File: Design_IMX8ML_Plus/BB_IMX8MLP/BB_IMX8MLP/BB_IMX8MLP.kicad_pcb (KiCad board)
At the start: 2 copper layers, 6 parts, among them J1 DF40C-100DP-0.4V_51_, J2 DF40C-100DP-0.4V_51_, J3 DF40C-100DP-0.4V_51_, J4 DF40C-100DP-0.4V_51_, J5 RJ45_Amphenol_RJMG1BD3B8K1ANR, J6 RJ45_Amphenol_RJMG1BD3B8K1ANR

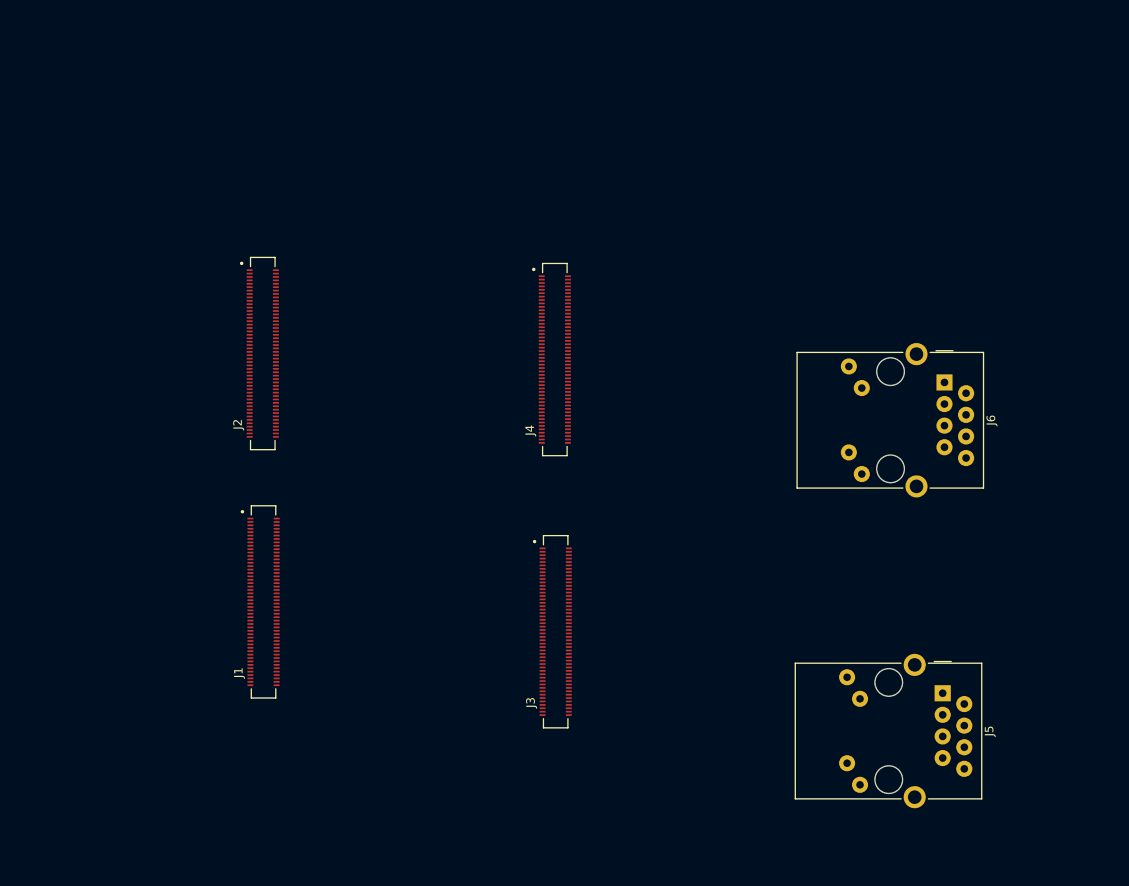
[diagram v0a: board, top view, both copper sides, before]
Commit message: Add SPB228 WIFI/BLE module
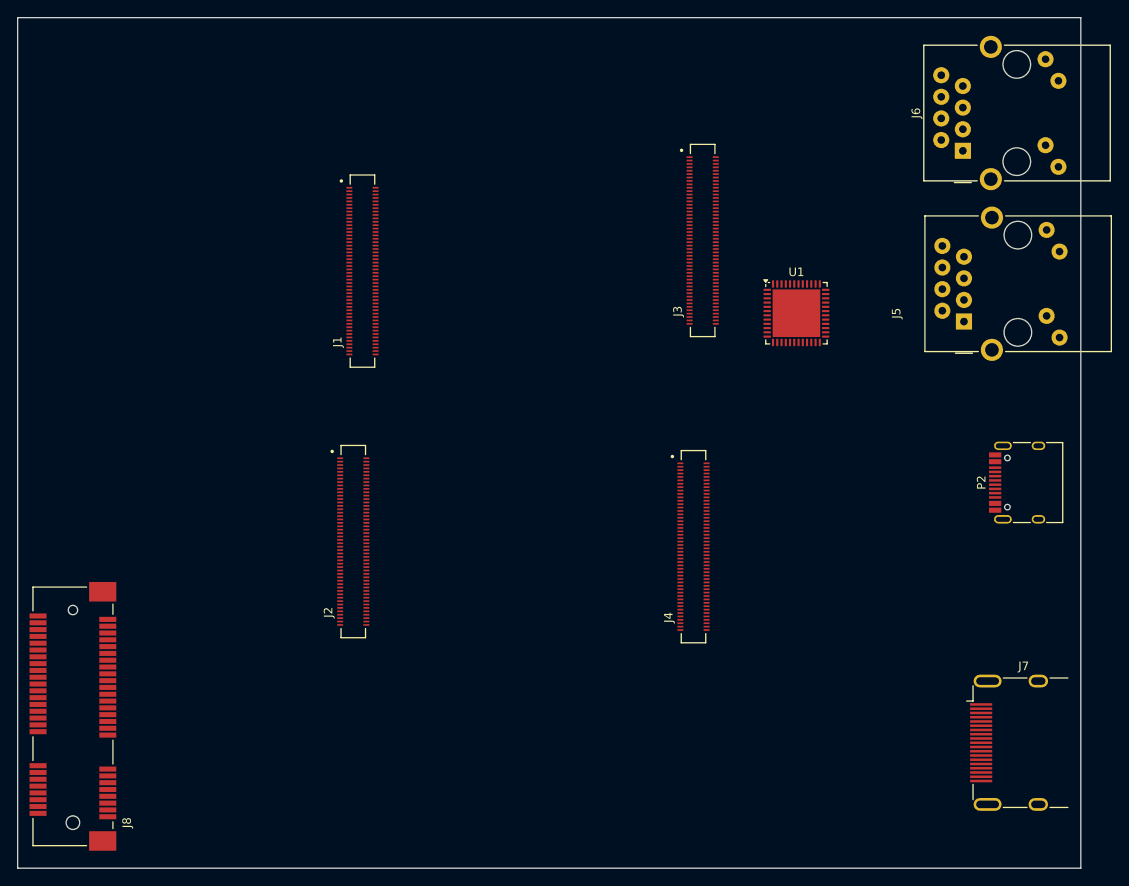
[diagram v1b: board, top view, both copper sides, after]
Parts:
- added J7: HDMI_A, Connector_Video:HDMI_A_Molex_208658-1001_Horizontal, F.Cu at (186.6, 135.2)
- added J8: Bus_PCI_Express_Mini, Connector_PCBEdge:BUS_PCI_Express_Mini, F.Cu at (76.5, 132.2)
- added P2: USB_C_Plug, Connector_USB:USB_C_Receptacle_HRO_TYPE-C-31-M-12, F.Cu at (189.0, 104.7)
- added U1: KSZ9131RNXI, Package_DFN_QFN:QFN-48-1EP_7x7mm_P0.5mm_EP5.6x5.6mm, F.Cu at (161.6, 84.8)
- moved J3 49.1 mm to (150.5, 76.2)
- moved J5 43.8 mm to (181.3, 85.7), turned to 90 degrees
- moved J1 40.6 mm to (110.5, 79.8)
- moved J4 27.4 mm to (149.5, 112.2)
- moved J6 27.3 mm to (181.1, 65.7), turned to 90 degrees
- moved J2 24.5 mm to (109.5, 111.6)
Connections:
- J1 pad 29: unconnected-(J1-Pad29) -> SAI1_RXD5
- J1 pad 31: unconnected-(J1-Pad31) -> SAI1_RXD6
- J1 pad 32: unconnected-(J1-Pad32) -> SAI5_RXD0
- J1 pad 33: unconnected-(J1-Pad33) -> SAI1_RXD7
- J1 pad 34: unconnected-(J1-Pad34) -> SAI5_RXD1
- J1 pad 35: unconnected-(J1-Pad35) -> SAI1_TXD0
- J1 pad 36: unconnected-(J1-Pad36) -> SAI5_RXD2
- J1 pad 37: unconnected-(J1-Pad37) -> SAI1_TXD1
- J1 pad 38: unconnected-(J1-Pad38) -> SAI5_RXD3
- J1 pad 39: unconnected-(J1-Pad39) -> SAI1_TXD2
- J1 pad 40: unconnected-(J1-Pad40) -> SAI5_MCLK
- J1 pad 41: unconnected-(J1-Pad41) -> SAI1_TXD3
- J1 pad 42: unconnected-(J1-Pad42) -> SAI5_RXC
- J1 pad 43: unconnected-(J1-Pad43) -> SAI1_TXD4
- J1 pad 44: unconnected-(J1-Pad44) -> SAI5_RXFS
- J1 pad 45: unconnected-(J1-Pad45) -> SAI1_TXD5
- J1 pad 47: unconnected-(J1-Pad47) -> SAI1_TXD6
- J1 pad 49: unconnected-(J1-Pad49) -> SAI1_RXD7
- J1 pad 60: unconnected-(J1-Pad60) -> LED1
- J1 pad 62: unconnected-(J1-Pad62) -> LED2
- J1 pad 66: unconnected-(J1-Pad66) -> TXRXA_N
- J1 pad 68: unconnected-(J1-Pad68) -> TXRXA_P
- J1 pad 72: unconnected-(J1-Pad72) -> TXRXB_N
- J1 pad 74: unconnected-(J1-Pad74) -> TXRXB_P
- J1 pad 78: unconnected-(J1-Pad78) -> TXRXC_P
- J1 pad 80: unconnected-(J1-Pad80) -> TXRXC_N
- J1 pad 84: unconnected-(J1-Pad84) -> TXRXD_N
- J1 pad 86: unconnected-(J1-Pad86) -> TXRXD_P
- J2 pad 10: unconnected-(J2-Pad10) -> SAI2_MCLK
- J2 pad 11: unconnected-(J2-Pad11) -> SAI1_MCLK
- J2 pad 12: unconnected-(J2-Pad12) -> SAI2_RXC
- J2 pad 13: unconnected-(J2-Pad13) -> SAI1_RXC
- J2 pad 14: unconnected-(J2-Pad14) -> SAI2_RXFS
- J2 pad 15: unconnected-(J2-Pad15) -> SAI1_RXFS
- J2 pad 16: unconnected-(J2-Pad16) -> SAI2_TXC
- J2 pad 17: unconnected-(J2-Pad17) -> SAI1_TXC
- J2 pad 18: unconnected-(J2-Pad18) -> SAI2_TXFS
- J2 pad 19: unconnected-(J2-Pad19) -> SAi1_TXFS
- J2 pad 21: unconnected-(J2-Pad21) -> I2C1_SCL
- J2 pad 22: unconnected-(J2-Pad22) -> SAI2_RXD0
- J2 pad 23: unconnected-(J2-Pad23) -> I2C1_SDA
- J2 pad 24: unconnected-(J2-Pad24) -> SAI2_TXD0
- J2 pad 27: unconnected-(J2-Pad27) -> I2C3_SDA
- J2 pad 28: unconnected-(J2-Pad28) -> SAI3_MCLK
- J2 pad 29: unconnected-(J2-Pad29) -> I2C3_SCL
- J2 pad 30: unconnected-(J2-Pad30) -> SAI3_RXC
- J2 pad 32: unconnected-(J2-Pad32) -> SAI3_RXD
- J2 pad 33: unconnected-(J2-Pad33) -> I2C2_SCL
- J2 pad 34: unconnected-(J2-Pad34) -> SAI3_RXFS
- J2 pad 35: unconnected-(J2-Pad35) -> I2C2_SDA
- J2 pad 36: unconnected-(J2-Pad36) -> SAI3_TXC
- J2 pad 38: unconnected-(J2-Pad38) -> SAI3_TXD
- J2 pad 39: unconnected-(J2-Pad39) -> I2C4_SDA
- J2 pad 40: unconnected-(J2-Pad40) -> SAI3_TXFS
- J2 pad 41: unconnected-(J2-Pad41) -> I2C4_SCL
- J2 pad 45: unconnected-(J2-Pad45) -> UART1_RXD
- J2 pad 47: unconnected-(J2-Pad47) -> UART1_TXD
- J2 pad 48: unconnected-(J2-Pad48) -> SAI1_RXD0
- J2 pad 49: unconnected-(J2-Pad49) -> UART2_RXD
- J2 pad 50: unconnected-(J2-Pad50) -> SAI1_RXD1
- J2 pad 51: unconnected-(J2-Pad51) -> UART2_TXD
- J2 pad 52: unconnected-(J2-Pad52) -> SAI1_RXD2
- J2 pad 53: unconnected-(J2-Pad53) -> UART3_RXD
- J2 pad 54: unconnected-(J2-Pad54) -> SAI1_RXD3
- J2 pad 55: unconnected-(J2-Pad55) -> UART3_TXD
- J2 pad 56: unconnected-(J2-Pad56) -> SAI1_RXD4
- J2 pad 57: unconnected-(J2-Pad57) -> UART4_RXD
- J2 pad 59: unconnected-(J2-Pad59) -> UART4_TXD
- J2 pad 65: unconnected-(J2-Pad65) -> CSI1_CLK_P
- J2 pad 67: unconnected-(J2-Pad67) -> CSI1_CLK_N
- J2 pad 71: unconnected-(J2-Pad71) -> CSI2_CLK_P
- J2 pad 73: unconnected-(J2-Pad73) -> CSI2_CLK_N
- J2 pad 77: unconnected-(J2-Pad77) -> DSI1_CLK_P
- J2 pad 79: unconnected-(J2-Pad79) -> DSI1_CLK_N
- J2 pad 80: unconnected-(J2-Pad80) -> ECSPI1_MISO
- J2 pad 82: unconnected-(J2-Pad82) -> ECSPI1_MOSI
- J2 pad 84: unconnected-(J2-Pad84) -> ECSPI1_SCLK
- J2 pad 85: unconnected-(J2-Pad85) -> EARC_AUX
- J2 pad 86: unconnected-(J2-Pad86) -> ECSPI1_SSO
- J2 pad 87: unconnected-(J2-Pad87) -> EARC_N_HPD
- J2 pad 88: unconnected-(J2-Pad88) -> ECSPI2_MISO
- J2 pad 89: unconnected-(J2-Pad89) -> EARC_P_UTIL
- J2 pad 90: unconnected-(J2-Pad90) -> ECSPI2_MOSI
- J2 pad 92: unconnected-(J2-Pad92) -> ECSPI2_SCLK
- J2 pad 94: unconnected-(J2-Pad94) -> ECSPI2_SSO
- J3 pad 100: unconnected-(J3-Pad100) -> VDD_SYS
- J3 pad 11: unconnected-(J3-Pad11) -> PCIE_TXN_P
- J3 pad 13: unconnected-(J3-Pad13) -> PCIE_TXN_N
- J3 pad 15: unconnected-(J3-Pad15) -> PCIE_RXN_P
- J3 pad 17: unconnected-(J3-Pad17) -> PCIE_RXN_N
- J3 pad 21: unconnected-(J3-Pad21) -> PCIE_REF_PAD_CLK_P
- J3 pad 23: unconnected-(J3-Pad23) -> PCIE_REF_PAD_CLK_N
- J3 pad 33: unconnected-(J3-Pad33) -> GPIO1_IO00
- J3 pad 35: unconnected-(J3-Pad35) -> GPIO1_IO01
- J3 pad 37: unconnected-(J3-Pad37) -> GPIO1_IO02
- J3 pad 43: unconnected-(J3-Pad43) -> GPIO1_IO05
- J3 pad 45: unconnected-(J3-Pad45) -> GPIO1_IO06
- J3 pad 47: unconnected-(J3-Pad47) -> GPIO1_IO07
- J3 pad 49: unconnected-(J3-Pad49) -> GPIO1_IO08
- J3 pad 51: unconnected-(J3-Pad51) -> GPIO1_IO09
- J3 pad 53: unconnected-(J3-Pad53) -> GPIO1_IO10
- J3 pad 55: unconnected-(J3-Pad55) -> GPIO1_IO11
- J3 pad 57: unconnected-(J3-Pad57) -> GPIO1_IO12
- J3 pad 59: unconnected-(J3-Pad59) -> GPIO1_IO13
- J3 pad 61: unconnected-(J3-Pad61) -> GPIO1_IO14
- J3 pad 63: unconnected-(J3-Pad63) -> GPIO1_IO15
- J3 pad 75: unconnected-(J3-Pad75) -> GND
- J3 pad 76: unconnected-(J3-Pad76) -> GND
- J3 pad 77: unconnected-(J3-Pad77) -> GND
- J3 pad 78: unconnected-(J3-Pad78) -> GND
- J3 pad 79: unconnected-(J3-Pad79) -> GND
- J3 pad 80: unconnected-(J3-Pad80) -> GND
- J3 pad 81: unconnected-(J3-Pad81) -> GND
- J3 pad 82: unconnected-(J3-Pad82) -> GND
- J3 pad 83: unconnected-(J3-Pad83) -> GND
- J3 pad 84: unconnected-(J3-Pad84) -> GND
- J3 pad 85: unconnected-(J3-Pad85) -> GND
- J3 pad 86: unconnected-(J3-Pad86) -> GND
- J3 pad 87: unconnected-(J3-Pad87) -> GND
- J3 pad 88: unconnected-(J3-Pad88) -> GND
- J3 pad 89: unconnected-(J3-Pad89) -> VDD_SYS
- J3 pad 90: unconnected-(J3-Pad90) -> VDD_SYS
- J3 pad 91: unconnected-(J3-Pad91) -> VDD_SYS
- J3 pad 92: unconnected-(J3-Pad92) -> VDD_SYS
- J3 pad 93: unconnected-(J3-Pad93) -> VDD_SYS
- J3 pad 94: unconnected-(J3-Pad94) -> VDD_SYS
- J3 pad 95: unconnected-(J3-Pad95) -> VDD_SYS
- J3 pad 96: unconnected-(J3-Pad96) -> VDD_SYS
- J3 pad 97: unconnected-(J3-Pad97) -> VDD_SYS
- J3 pad 98: unconnected-(J3-Pad98) -> VDD_SYS
- J3 pad 99: unconnected-(J3-Pad99) -> VDD_SYS
- J4 pad 10: unconnected-(J4-Pad10) -> JTAG_TMS
- J4 pad 11: unconnected-(J4-Pad11) -> HDM_TX2_N
- J4 pad 12: unconnected-(J4-Pad12) -> JTAG_TDO
- J4 pad 13: unconnected-(J4-Pad13) -> HDM_TX1_P
- J4 pad 14: unconnected-(J4-Pad14) -> JTAG_TDI
- J4 pad 15: unconnected-(J4-Pad15) -> HDM_TX1_N
- J4 pad 16: unconnected-(J4-Pad16) -> JTAG_TCK
- J4 pad 17: unconnected-(J4-Pad17) -> HDM_TX0_P
- J4 pad 18: unconnected-(J4-Pad18) -> JTAG_MOD
- J4 pad 19: unconnected-(J4-Pad19) -> HDM_TX0_N
- J4 pad 22: unconnected-(J4-Pad22) -> CLKOUT2
- J4 pad 23: unconnected-(J4-Pad23) -> HDM_HPD
- J4 pad 24: unconnected-(J4-Pad24) -> CLKOUT1
- J4 pad 25: unconnected-(J4-Pad25) -> HDM_DDC_SDA
- J4 pad 26: unconnected-(J4-Pad26) -> CLKIN2
- J4 pad 27: unconnected-(J4-Pad27) -> HDM_DDC_SCL
- J4 pad 28: unconnected-(J4-Pad28) -> CLKIN1
- J4 pad 29: unconnected-(J4-Pad29) -> HDM_CEC
- J4 pad 32: unconnected-(J4-Pad32) -> BOOT_MODE3
- J4 pad 34: unconnected-(J4-Pad34) -> BOOT_MODE2
- J4 pad 36: unconnected-(J4-Pad36) -> BOOT_MODE1
- J4 pad 37: unconnected-(J4-Pad37) -> LVDS1_CLK_N
- J4 pad 38: unconnected-(J4-Pad38) -> BOOT_MODE0
- J4 pad 39: unconnected-(J4-Pad39) -> LVDS1_CLK_P
- J4 pad 41: unconnected-(J4-Pad41) -> LVDS1_D3_P
- J4 pad 43: unconnected-(J4-Pad43) -> LVDS1_D3_N
- J4 pad 44: unconnected-(J4-Pad44) -> SDC1_STROBE
- J4 pad 45: unconnected-(J4-Pad45) -> LVDS1_D2_P
- J4 pad 46: unconnected-(J4-Pad46) -> SDC1_RESET_B
- J4 pad 47: unconnected-(J4-Pad47) -> LVDS1_D2_N
- J4 pad 48: unconnected-(J4-Pad48) -> SDC1_DATA7
- J4 pad 49: unconnected-(J4-Pad49) -> LVDS1_D1_P
- J4 pad 5: unconnected-(J4-Pad5) -> HDM_TXC_P
- J4 pad 50: unconnected-(J4-Pad50) -> SDC1_DATA6
- J4 pad 51: unconnected-(J4-Pad51) -> LVDS1_D1_N
- J4 pad 52: unconnected-(J4-Pad52) -> SDC1_DATA5
- J4 pad 53: unconnected-(J4-Pad53) -> LVDS1_D0_P
- J4 pad 54: unconnected-(J4-Pad54) -> SDC1_DATA4
- J4 pad 55: unconnected-(J4-Pad55) -> LVDS1_D0_N
- J4 pad 56: unconnected-(J4-Pad56) -> SDC1_DATA3
- J4 pad 58: unconnected-(J4-Pad58) -> SDC1_DATA2
- J4 pad 59: unconnected-(J4-Pad59) -> LVDS0_CLK_P
- J4 pad 60: unconnected-(J4-Pad60) -> SDC1_DATA1
- J4 pad 61: unconnected-(J4-Pad61) -> LVDS0_CLK_N
- J4 pad 62: unconnected-(J4-Pad62) -> SDC1_DATA0
- J4 pad 63: unconnected-(J4-Pad63) -> LVDS0_D3_P
- J4 pad 64: unconnected-(J4-Pad64) -> SDC1_CMD
- J4 pad 65: unconnected-(J4-Pad65) -> LVDS0_D3_N
- J4 pad 66: unconnected-(J4-Pad66) -> SDC1_CLK
- J4 pad 67: unconnected-(J4-Pad67) -> LVDS0_D2_P
- J4 pad 69: unconnected-(J4-Pad69) -> LVDS0_D2_N
- J4 pad 7: unconnected-(J4-Pad7) -> HDM_TXC_N
- J4 pad 70: unconnected-(J4-Pad70) -> SDC2_WP
- J4 pad 71: unconnected-(J4-Pad71) -> LVDS0_D1_P
- J4 pad 72: unconnected-(J4-Pad72) -> SDC2_RESET_B
- J4 pad 73: unconnected-(J4-Pad73) -> LVDS0_D1_N
- J4 pad 74: unconnected-(J4-Pad74) -> SDC2_DATA3
- J4 pad 75: unconnected-(J4-Pad75) -> LVDS0_D0_P
- J4 pad 76: unconnected-(J4-Pad76) -> SDC2_DATA2
- J4 pad 77: unconnected-(J4-Pad77) -> LVDS0_D0_N
- J4 pad 78: unconnected-(J4-Pad78) -> SDC2_DATA1
- J4 pad 80: unconnected-(J4-Pad80) -> SDC2_DATA0
- J4 pad 82: unconnected-(J4-Pad82) -> SDC2_CMD
- J4 pad 84: unconnected-(J4-Pad84) -> SDC2_CLK
- J4 pad 86: unconnected-(J4-Pad86) -> SDC2_CD_B
- J4 pad 9: unconnected-(J4-Pad9) -> HDM_TX2_P
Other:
- board outline added: 125 x 100 mm

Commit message: Improve power source module in the base board
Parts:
- added C1: 16Pf, Capacitor_SMD:C_0402_1005Metric, F.Cu at (168.2, 120.0)
- added C10: 100nF, Capacitor_SMD:C_0402_1005Metric, B.Cu at (66.4, 171.0)
- added C11: 10uF, Capacitor_SMD:C_0402_1005Metric, F.Cu at (63.0, 177.0)
- added C12: 100nF, Capacitor_SMD:C_0402_1005Metric, F.Cu at (64.0, 178.7)
- added C13: 1uF, Capacitor_SMD:C_0402_1005Metric, F.Cu at (70.1, 176.5)
- added C14: 10uF, Capacitor_SMD:C_0402_1005Metric, F.Cu at (67.5, 161.1)
- added C15: 10uF, Capacitor_SMD:C_0402_1005Metric, F.Cu at (67.4, 162.4)
- added C16: 10uF, Capacitor_SMD:C_0402_1005Metric, F.Cu at (67.4, 163.7)
- added C17: 47uF, Capacitor_SMD:C_0402_1005Metric, F.Cu at (41.2, 183.8)
- added C18: 47uF, Capacitor_SMD:C_0402_1005Metric, F.Cu at (41.1, 182.6)
- added C19: 47uF, Capacitor_SMD:C_0402_1005Metric, F.Cu at (41.1, 181.4)
- added C2: 16Pf, Capacitor_SMD:C_0402_1005Metric, F.Cu at (165.4, 120.3)
- added C20: 10uF, Capacitor_SMD:C_0402_1005Metric, F.Cu at (82.5, 174.8)
- added C21: 47uF, Capacitor_SMD:C_0402_1005Metric, F.Cu at (118.8, 174.4)
- added C22: 47uF, Capacitor_SMD:C_0402_1005Metric, F.Cu at (118.8, 176.4)
- added C23: 47uF, Capacitor_SMD:C_0402_1005Metric, F.Cu at (118.8, 178.3)
- added C24: 47uF, Capacitor_SMD:C_0402_1005Metric, F.Cu at (118.8, 180.3)
- added C25: 4.7uF, Capacitor_SMD:C_0402_1005Metric, F.Cu at (118.8, 182.3)
- added C26: 100nF, Capacitor_SMD:C_0402_1005Metric, F.Cu at (118.8, 184.2)
- added C27: 100nF, Capacitor_SMD:C_0402_1005Metric, F.Cu at (118.8, 186.2)
- added C28: 100nF, Capacitor_SMD:C_0402_1005Metric, B.Cu at (84.3, 135.4)
- added C3: 47uF, Capacitor_SMD:C_0402_1005Metric, F.Cu at (41.1, 185.0)
- added C4: 100nF, Capacitor_SMD:C_0402_1005Metric, F.Cu at (82.2, 167.8)
- added C5: 10uF, Capacitor_SMD:C_0402_1005Metric, B.Cu at (77.1, 164.8)
- added C6: 10uF, Capacitor_SMD:C_0402_1005Metric, F.Cu at (75.2, 177.5)
- added C7: 100nF, Capacitor_SMD:C_0402_1005Metric, F.Cu at (56.0, 186.0)
- added C8: 100nF, Capacitor_SMD:C_0402_1005Metric, B.Cu at (58.9, 185.9)
- added C9: 4.7uF, Capacitor_SMD:C_0402_1005Metric, F.Cu at (58.1, 186.7)
- added D1: SS3200, Diode_SMD:D_SMA, F.Cu at (80.6, 177.9)
- added D2: GREEN, LED_SMD:LED_0402_1005Metric, F.Cu at (85.5, 127.3)
- added D3: GREEN, LED_SMD:LED_0402_1005Metric, F.Cu at (85.5, 125.3)
- added D4: GREEN, LED_SMD:LED_0402_1005Metric, F.Cu at (85.5, 123.3)
- added F1: 10A 36R@100MHz, Fuse:Fuse_0603_1608Metric, F.Cu at (79.5, 175.0)
- added J10: Barrel_Jack, Connector_BarrelJack:BarrelJack_CUI_PJ-063AH_Horizontal, F.Cu at (78.3, 181.7)
- added J11: SIM_Card, Connector_Card:nanoSIM_Hinged_CUI_NSIM-2-C, B.Cu at (93.0, 139.5)
- added J9: GSB311231HR, _W_SBC:AMPHENOL_GSB311231HR, F.Cu at (183.8, 115.1)
- added L1: 2.2uH_12A, Inductor_SMD:L_7.3x7.3_H3.5, F.Cu at (47.5, 182.9)
- added L2: 2.2uH_12A, Inductor_SMD:L_7.3x7.3_H3.5, F.Cu at (124.9, 177.8)
- added Q1: PMDT290UCE, Package_TO_SOT_SMD:SOT-666, F.Cu at (66.7, 182.5)
- added Q2: NTMFS5C670NLT1G, _W_SBC:NTMFS5C670NLT1G_ONS, F.Cu at (72.8, 162.9)
- added Q3: NTMFS5C670NLT1G, _W_SBC:NTMFS5C670NLT1G_ONS, F.Cu at (82.0, 162.6)
- added Q4: PMDT290UCE, Package_TO_SOT_SMD:SOT-666, F.Cu at (128.1, 184.1)
- added R1: 47K, Resistor_SMD:R_0402_1005Metric, B.Cu at (58.8, 181.8)
- added R10: 100K, Resistor_SMD:R_0402_1005Metric, F.Cu at (84.4, 171.2)
- added R11: 787K, Resistor_SMD:R_0402_1005Metric, F.Cu at (84.4, 170.0)
- added R12: 80.6K, Resistor_SMD:R_0402_1005Metric, F.Cu at (84.4, 168.6)
- added R13: 18.2K, Resistor_SMD:R_0402_1005Metric, F.Cu at (84.4, 167.5)
- added R14: 80.6K, Resistor_SMD:R_0402_1005Metric, B.Cu at (79.0, 164.8)
- added R15: 0.01, Resistor_SMD:R_0402_1005Metric, F.Cu at (67.4, 164.8)
- added R16: 100K, Resistor_SMD:R_0402_1005Metric, F.Cu at (115.9, 174.4)
- added R17: 100K, Resistor_SMD:R_0402_1005Metric, F.Cu at (115.9, 176.4)
- added R18: 100K, Resistor_SMD:R_0402_1005Metric, F.Cu at (115.9, 178.4)
- added R19: 47K, Resistor_SMD:R_0402_1005Metric, F.Cu at (115.9, 180.4)
- added R2: 8.87K, Resistor_SMD:R_0402_1005Metric, B.Cu at (58.8, 180.6)
- added R20: 8.87K, Resistor_SMD:R_0402_1005Metric, F.Cu at (115.9, 182.4)
- added R21: 100K, Resistor_SMD:R_0402_1005Metric, F.Cu at (115.9, 184.3)
- added R22: 510K, Resistor_SMD:R_0402_1005Metric, F.Cu at (115.9, 186.3)
- added R23: 100K, Resistor_SMD:R_0402_1005Metric, F.Cu at (115.9, 188.3)
- added R24: 100K, Resistor_SMD:R_0402_1005Metric, F.Cu at (88.7, 127.3)
- added R25: 100K, Resistor_SMD:R_0402_1005Metric, F.Cu at (88.7, 125.3)
- added R26: 100K, Resistor_SMD:R_0402_1005Metric, F.Cu at (88.7, 123.3)
- added R3: 100K, Resistor_SMD:R_0402_1005Metric, F.Cu at (58.1, 185.6)
- added R4: 100K, Resistor_SMD:R_0402_1005Metric, F.Cu at (61.8, 182.3)
- added R5: 100K, Resistor_SMD:R_0402_1005Metric, F.Cu at (63.2, 184.3)
- added R6: 510K, Resistor_SMD:R_0402_1005Metric, F.Cu at (59.0, 178.8)
- added R7: 100K, Resistor_SMD:R_0402_1005Metric, F.Cu at (66.2, 178.7)
- added R8: 100K, Resistor_SMD:R_0402_1005Metric, F.Cu at (70.6, 183.3)
- added R9: 100K, Resistor_SMD:R_0402_1005Metric, F.Cu at (70.6, 182.0)
- added SW1: Power ON/OFF, Button_Switch_SMD:SW_SPST_TL3342, F.Cu at (95.9, 174.3)
- added SW2: RESET, Button_Switch_SMD:SW_SPST_TL3342, F.Cu at (95.9, 181.3)
- added SW3: RECOVERY, Button_Switch_SMD:SW_SPST_TL3342, F.Cu at (95.9, 188.4)
- added U2: HDMI2C1-14HDS, Package_DFN_QFN:VQFN-24-1EP_4x4mm_P0.5mm_EP2.5x2.5mm, F.Cu at (168.7, 130.4)
- added U3: USB5744_2G, _W_SBC:QFN40P700X700X100-57N, F.Cu at (165.3, 113.7)
- added U4: LTC4368IDD-1_PBF, Package_DFN_QFN:DFN-10-1EP_3x3mm_P0.5mm_EP1.65x2.38mm, F.Cu at (80.2, 170.2)
- added U5: AOZ2261AQI-15, _W_SBC:QFN4X4-22L_EP2_S_AOS, F.Cu at (57.3, 182.3)
- added U6: NCV4274CST50T3G, Package_TO_SOT_SMD:SOT-223, B.Cu at (60.0, 171.4)
- added U7: AOZ2261AQI-15, _W_SBC:QFN4X4-22L_EP2_S_AOS, F.Cu at (123.1, 185.3)
- added U8: LTC2954CDDB-1-TRMPBF, _W_SBC:DFN-8_DDB_LIT, F.Cu at (66.2, 176.2)
- added Y1: 25MHz, Crystal:Crystal_SMD_0603-4Pin_6.0x3.5mm, F.Cu at (166.9, 123.6)
- moved J7 18.4 mm to (169.7, 142.5), turned to -90 degrees
- moved P2 5.49 mm to (191.1, 99.6)
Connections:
- J7 pad 1: unconnected-(J7-D2+-Pad1) -> Net-(J7-D2+)
- J7 pad 10: unconnected-(J7-CK+-Pad10) -> Net-(J7-CK+)
- J7 pad 12: unconnected-(J7-CK--Pad12) -> Net-(J7-CK-)
- J7 pad 3: unconnected-(J7-D2--Pad3) -> Net-(J7-D2-)
- J7 pad 4: unconnected-(J7-D1+-Pad4) -> Net-(J7-D1+)
- J7 pad 6: unconnected-(J7-D1--Pad6) -> Net-(J7-D1-)
- J7 pad 7: unconnected-(J7-D0+-Pad7) -> Net-(J7-D0+)
- J7 pad 9: unconnected-(J7-D0--Pad9) -> Net-(J7-D0-)
- J8 pad 10: unconnected-(J8-UIM_DATA-Pad10) -> Net-(J11-I/O)
- J8 pad 12: unconnected-(J8-UIM_CLK-Pad12) -> Net-(J11-CLK)
- J8 pad 14: unconnected-(J8-~{UIM_RESET}-Pad14) -> Net-(J11-RST)
- J8 pad 16: unconnected-(J8-UIM_VPP-Pad16) -> Net-(J11-VPP)
- J8 pad 2: unconnected-(J8-+3V3AUX-Pad2) -> Net-(J8-+3V3AUX-Pad2)
- J8 pad 24: unconnected-(J8-+3V3AUX-Pad24) -> Net-(J8-+3V3AUX-Pad2)
- J8 pad 36: unconnected-(J8-USB_D--Pad36) -> USBDN_D3-
- J8 pad 38: unconnected-(J8-USB_D+-Pad38) -> USBDN_D3+
- J8 pad 39: unconnected-(J8-+3V3AUX-Pad39) -> Net-(J8-+3V3AUX-Pad2)
- J8 pad 41: unconnected-(J8-+3V3AUX-Pad41) -> Net-(J8-+3V3AUX-Pad2)
- J8 pad 42: unconnected-(J8-~{LED_WWAN}-Pad42) -> Net-(D4-K)
- J8 pad 44: unconnected-(J8-~{LED_WLAN}-Pad44) -> Net-(D3-K)
- J8 pad 46: unconnected-(J8-~{LED_WPAN}-Pad46) -> Net-(D2-K)
- J8 pad 52: unconnected-(J8-+3V3AUX-Pad52) -> Net-(J8-+3V3AUX-Pad2)
- J8 pad 8: unconnected-(J8-UIM_PWR-Pad8) -> Net-(J11-VCC)
- U1 pad 10: TXRXD_P -> unconnected-(U1A-TXRXP_D-Pad10)
- U1 pad 11: TXRXD_N -> unconnected-(U1A-TXRXM_D-Pad11)
- U1 pad 15: LED2 -> unconnected-(U1A-LED2/PHYAD1-Pad15)
- U1 pad 17: LED1 -> unconnected-(U1A-LED1/PME_N1//PHYAD0-Pad17)
- U1 pad 19: ENET_TD0 -> unconnected-(U1A-TXD0-Pad19)
- U1 pad 2: TXRXA_P -> unconnected-(U1A-TXRXP_A-Pad2)
- U1 pad 20: ENET_TD1 -> unconnected-(U1A-TXD1-Pad20)
- U1 pad 21: ENET_TD2 -> unconnected-(U1A-TXD2-Pad21)
- U1 pad 22: ENET_TD3 -> unconnected-(U1A-TXD3-Pad22)
- U1 pad 24: ENET_TXC -> unconnected-(U1A-TXC-Pad24)
- U1 pad 25: ENET_TX_CTL -> unconnected-(U1A-TX_CTL-Pad25)
- U1 pad 27: ENET_RD3 -> unconnected-(U1A-RXD3/MODE3-Pad27)
- U1 pad 28: ENET_RD2 -> unconnected-(U1A-RXD2/MODE2-Pad28)
- U1 pad 3: TXRXA_N -> unconnected-(U1A-TXRXM_A-Pad3)
- U1 pad 31: ENET_RD1 -> unconnected-(U1A-RXD1/MODE1-Pad31)
- U1 pad 32: ENET_RD0 -> unconnected-(U1A-RXD0/MODE0-Pad32)
- U1 pad 33: ENET_RX_CTL -> unconnected-(U1A-RX_CTL/CLK125_EN-Pad33)
- U1 pad 35: ENET_RXC -> unconnected-(U1A-RXC/PHYAD2-Pad35)
- U1 pad 36: ENET_MDC -> unconnected-(U1A-MDC-Pad36)
- U1 pad 37: ENET_MDIO -> unconnected-(U1A-MDIO-Pad37)
- U1 pad 5: TXRXB_P -> unconnected-(U1A-TXRXP_B-Pad5)
- U1 pad 6: TXRXB_N -> unconnected-(U1A-TXRXM_B-Pad6)
- U1 pad 7: TXRXC_P -> unconnected-(U1A-TXRXP_C-Pad7)
- U1 pad 8: TXRXC_N -> unconnected-(U1A-TXRXM_C-Pad8)
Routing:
- net /power_unit/+V_SUPPLY_FILT: track 0.00 -> 30.4 mm, vias 0 -> 2
- net Net-(U4-GATE): track 0.00 -> 30.2 mm, vias 0 -> 2
- net VDD_SYS: track 0.00 -> 23.0 mm, vias 0 -> 1
- net GND: track 0.00 -> 16.8 mm, vias 0 -> 2
- net Net-(U4-~{SHDN}): track 0.00 -> 15.9 mm, vias 0 -> 2
- net Net-(U4-SENSE): track 0.00 -> 14.7 mm
- net Net-(D1-K): track 0.00 -> 14.1 mm
- net Net-(C7-Pad2): track 0.00 -> 13.7 mm
- net /power_unit/5V_EN: track 0.00 -> 11.7 mm
- net /power_unit/+V5_STB: track 0.00 -> 11.1 mm, vias 0 -> 1
- net Net-(U4-VIN): track 0.00 -> 8.98 mm
- net Net-(Q1B-GP): track 0.00 -> 8.71 mm
- net Net-(Q2-Pad1): track 0.00 -> 8.45 mm
- net /power_unit/FB_5V: track 0.00 -> 7.73 mm, vias 0 -> 1
- net Net-(Q1B-DP): track 0.00 -> 7.37 mm
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
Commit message: improving the usb conector
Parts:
- removed P2: USB_C_Plug, Connector_USB:USB_C_Receptacle_HRO_TYPE-C-31-M-12
- added C29: 10uF, Capacitor_SMD:C_0402_1005Metric, F.Cu at (162.1, 119.2)
- added C30: 100nF, Capacitor_SMD:C_0402_1005Metric, F.Cu at (159.2, 113.9)
- added C31: 100nF, Capacitor_SMD:C_0402_1005Metric, F.Cu at (162.7, 107.5)
- added C32: 100nF, Capacitor_SMD:C_0402_1005Metric, F.Cu at (165.5, 107.8)
- added C33: 100nF, Capacitor_SMD:C_0402_1005Metric, F.Cu at (168.7, 108.0)
- added C34: 100nF, Capacitor_SMD:C_0402_1005Metric, F.Cu at (171.3, 111.9)
- added C35: 100nF, Capacitor_SMD:C_0402_1005Metric, F.Cu at (171.3, 114.7)
- added C36: 100nF, Capacitor_SMD:C_0402_1005Metric, F.Cu at (166.2, 119.3)
- added C37: 100nF, Capacitor_SMD:C_0402_1005Metric, F.Cu at (165.2, 119.3)
- added C38: 1nF, Capacitor_SMD:C_0402_1005Metric, F.Cu at (159.2, 115.0)
- added C39: 1nF, Capacitor_SMD:C_0402_1005Metric, F.Cu at (171.3, 115.7)
- added C40: 4.7uF, Capacitor_SMD:C_0402_1005Metric, F.Cu at (167.7, 107.9)
- added C41: 100nF, Capacitor_SMD:C_0402_1005Metric, F.Cu at (159.2, 111.8)
- added C42: 100nF, Capacitor_SMD:C_0402_1005Metric, F.Cu at (167.6, 119.4)
- added C43: 100nF, Capacitor_SMD:C_0402_1005Metric, F.Cu at (164.2, 119.3)
- added C44: 100nF, Capacitor_SMD:C_0402_1005Metric, F.Cu at (159.2, 112.8)
- added C45: 1nF, Capacitor_SMD:C_0402_1005Metric, F.Cu at (166.5, 107.8)
- added C46: 1nF, Capacitor_SMD:C_0402_1005Metric, F.Cu at (163.2, 119.2)
- added C47: 100nF, Capacitor_SMD:C_0402_1005Metric, F.Cu at (206.0, 110.6)
- added C48: 100nF, Capacitor_SMD:C_0402_1005Metric, F.Cu at (206.0, 112.6)
- added C49: 100nF, Capacitor_SMD:C_0402_1005Metric, F.Cu at (206.0, 114.6)
- added C50: 1nF, Capacitor_SMD:C_0402_1005Metric, F.Cu at (206.0, 116.5)
- added C51: 100nF, Capacitor_SMD:C_0402_1005Metric, F.Cu at (206.0, 118.5)
- added C52: 10uF, Capacitor_SMD:C_0402_1005Metric, F.Cu at (206.0, 120.5)
- added C53: 10uF, Capacitor_SMD:C_0402_1005Metric, F.Cu at (206.0, 122.5)
- added C54: 100nF, Capacitor_SMD:C_0402_1005Metric, F.Cu at (208.9, 110.6)
- added C55: 100nF, Capacitor_SMD:C_0402_1005Metric, F.Cu at (208.9, 112.6)
- added C56: 100nF, Capacitor_SMD:C_0402_1005Metric, F.Cu at (208.9, 114.6)
- added C57: 100nF, Capacitor_SMD:C_0402_1005Metric, F.Cu at (208.9, 116.5)
- added C58: 1nF, Capacitor_SMD:C_0402_1005Metric, F.Cu at (208.9, 118.5)
- added C59: 10uF, Capacitor_SMD:C_0402_1005Metric, F.Cu at (208.9, 120.5)
- added C60: 100nF, Capacitor_SMD:C_0402_1005Metric, F.Cu at (208.9, 122.5)
- added C61: 100nF, Capacitor_SMD:C_0402_1005Metric, F.Cu at (211.8, 110.6)
- added C62: 100nF, Capacitor_SMD:C_0402_1005Metric, F.Cu at (211.8, 112.6)
- added C63: 100nF, Capacitor_SMD:C_0402_1005Metric, F.Cu at (211.8, 114.6)
- added C64: 1nF, Capacitor_SMD:C_0402_1005Metric, F.Cu at (211.8, 116.5)
- added FB1: 220/100MHz, Resistor_SMD:R_0603_1608Metric, F.Cu at (215.2, 110.9)
- added FB2: 220/100MHz, Resistor_SMD:R_0603_1608Metric, F.Cu at (215.2, 113.4)
- added FB3: 220/100MHz, Resistor_SMD:R_0603_1608Metric, F.Cu at (215.2, 115.9)
- added P1: USB_C_Plug, Connector_USB:USB_C_Receptacle_HRO_TYPE-C-31-M-12, F.Cu at (191.3, 97.4)
- added R27: 47K, Resistor_SMD:R_0402_1005Metric, F.Cu at (214.7, 118.2)
- added U10: PCMF3USB3S, Package_CSP:Nexperia_WLCSP-15_6-3-6_2.37x1.17mm_Layout6x3_P0.4mm, B.Cu at (170.6, 112.2)
- added U11: ~, Package_DFN_QFN:DFN-12-1EP_3x3mm_P0.5mm_EP1.6x2.5mm, F.Cu at (202.0, 112.2)
- added U12: ~, Package_DFN_QFN:DFN-12-1EP_3x3mm_P0.5mm_EP1.6x2.5mm, F.Cu at (202.0, 117.1)
- added U13: ~, Package_DFN_QFN:DFN-12-1EP_3x3mm_P0.5mm_EP1.6x2.5mm, F.Cu at (202.0, 122.0)
- added U9: PCMF3USB3S, Package_CSP:Nexperia_WLCSP-15_6-3-6_2.37x1.17mm_Layout6x3_P0.4mm, B.Cu at (170.5, 117.9)
- moved C2 4.67 mm to (162.7, 124.2), turned to 90 degrees
- moved C1 3.60 mm to (170.8, 122.5)
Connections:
- J9 pad 11: /USB/USBDN_D2- -> Net-(J9B-D-_2)
- J9 pad 12: /USB/USBDN_D2+ -> Net-(J9B-D+_2)
- J9 pad 13: unconnected-(J9B-GND_2-Pad13) -> GND
- J9 pad 14: /USB/USB_SSRX_DN2- -> Net-(J9B-SSRX-_2)
- J9 pad 15: /USB/USB_SSRX_DN2+ -> Net-(J9B-SSRX+_2)
- J9 pad 17: /USB/USB_SSTX_DN2- -> Net-(J9B-SSTX-_2)
- J9 pad 18: /USB/USB_SSTX_DN2+ -> Net-(J9B-SSTX+_2)
- J9 pad 2: /USB/USBDN_D1- -> Net-(J9A-D-_1)
- J9 pad 3: /USB/USBDN_D1+ -> Net-(J9A-D+_1)
- J9 pad 5: /USB/USB_SSRX_DN1- -> Net-(J9A-SSRX-_1)
- J9 pad 6: /USB/USB_SSRX_DN1+ -> Net-(J9A-SSRX+_1)
- J9 pad 8: /USB/USB_SSTX_DN1- -> Net-(J9A-SSTX-_1)
- J9 pad 9: /USB/USB_SSTX_DN1+ -> Net-(J9A-SSTX+_1)
